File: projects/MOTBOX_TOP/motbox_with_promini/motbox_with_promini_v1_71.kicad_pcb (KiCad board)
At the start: 2 copper layers, 81.9 x 65 mm, 44 parts, among them J1 JST_XH_2pin, J2 JST_XH_3pin, J3 Conn_01x02, J4 JST_XH_4pin, J5 JST_XH_3pin, J6 JST_XH_3pin, J7 JST_XH_2pin, J8 Conn_02x03_Odd_Even, J9 Conn_01x02, U1 LM2576R-5.0, U2 L293D, U3 ATmega328P-AU, Y1 ABLS-16.000MHZ-B4-T

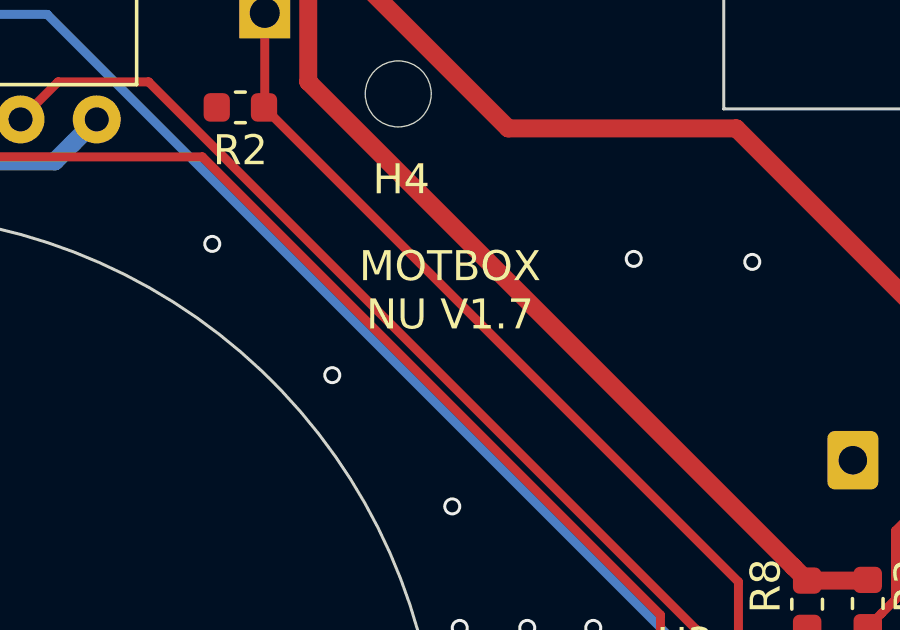
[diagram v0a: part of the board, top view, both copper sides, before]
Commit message: For transparent cable detection
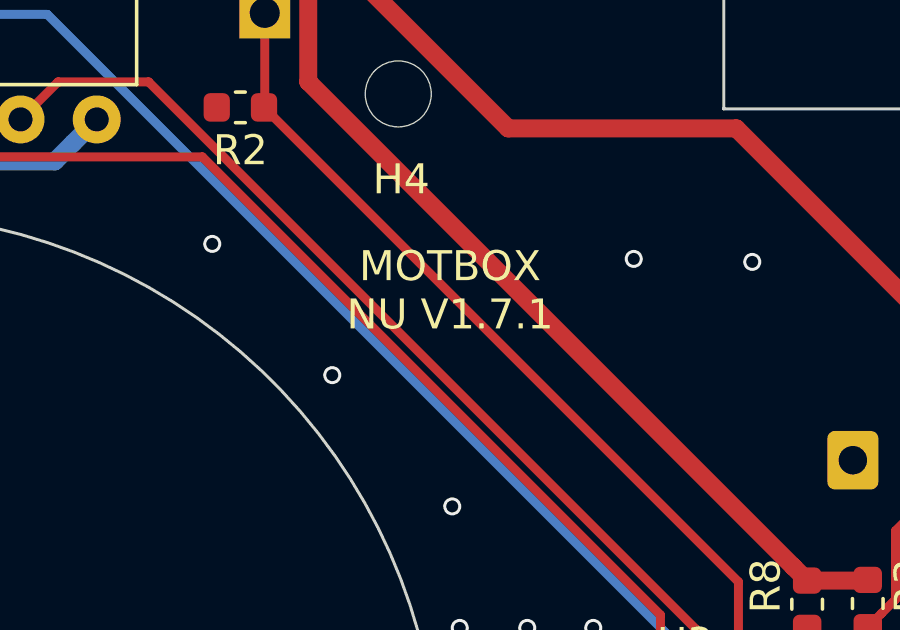
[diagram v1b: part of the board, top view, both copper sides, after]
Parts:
- R1, R3: value 60K -> 18K
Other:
- board text added: "MOTBOX NU V1.7.1"
- board text added: "Version 1.7.1 :Changing 60K to 18K the IR RX resistance"
- board text removed: "MOTBOX NU V1.7"
- board text removed: "Version 1.5 : Removing the promini and puttng the ATMEGA328P-AU"
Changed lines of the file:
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@@
       (psnegative false)
       (psa4output false)
-      (plotreference true)
+      (plotreference false)
       (plotvalue true)
       (plotinvisibletext false)
@@
       (effects (font (size 1 1) (thickness 0.15)))
     )
-    (fp_text value 60K (at 0 1.43 270) (layer F.Fab)
+    (fp_text value 18K (at 0 1.43 270) (layer F.Fab)
       (effects (font (size 1 1) (thickness 0.15)))
     )
@@
       (effects (font (size 1 1) (thickness 0.15)))
     )
-    (fp_text value 60K (at 0 1.43 270) (layer F.Fab)
+    (fp_text value 18K (at 0 1.43 270) (layer F.Fab)
       (effects (font (size 1 1) (thickness 0.15)))
     )
@@
     (effects (font (size 1 1) (thickness 0.25)) (justify mirror))
   )
-  (gr_text "MOTBOX\nNU V1.7" (at 158.275 48.95) (layer F.SilkS)
+  (gr_text "MOTBOX\nNU V1.7.1" (at 158.275 48.95) (layer F.SilkS)
     (effects (font (size 1 1) (thickness 0.25)))
   )
@@
     (effects (font (size 1 1) (thickness 0.25)) (justify mirror))
   )
-  (gr_text "Version 1.5  : Removing the promini and puttng the ATMEGA328P-AU" (at 228.3 172.25) (layer Cmts.User)
+  (gr_text "Version 1.7.1  :Changing 60K to 18K the IR RX resistance" (at 228.3 172.25) (layer Cmts.User)
     (effects (font (size 1.5 1.5) (thickness 0.3)))
   )

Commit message: Changes for improvments
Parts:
- R1, R3: value 18K -> 10K
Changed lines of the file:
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@@
       (effects (font (size 1 1) (thickness 0.15)))
     )
-    (fp_text value 18K (at 0 1.43 270) (layer F.Fab)
+    (fp_text value 10K (at 0 1.43 270) (layer F.Fab)
       (effects (font (size 1 1) (thickness 0.15)))
     )
@@
       (effects (font (size 1 1) (thickness 0.15)))
     )
-    (fp_text value 18K (at 0 1.43 270) (layer F.Fab)
+    (fp_text value 10K (at 0 1.43 270) (layer F.Fab)
       (effects (font (size 1 1) (thickness 0.15)))
     )
